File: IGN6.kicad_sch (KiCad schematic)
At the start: 24 parts

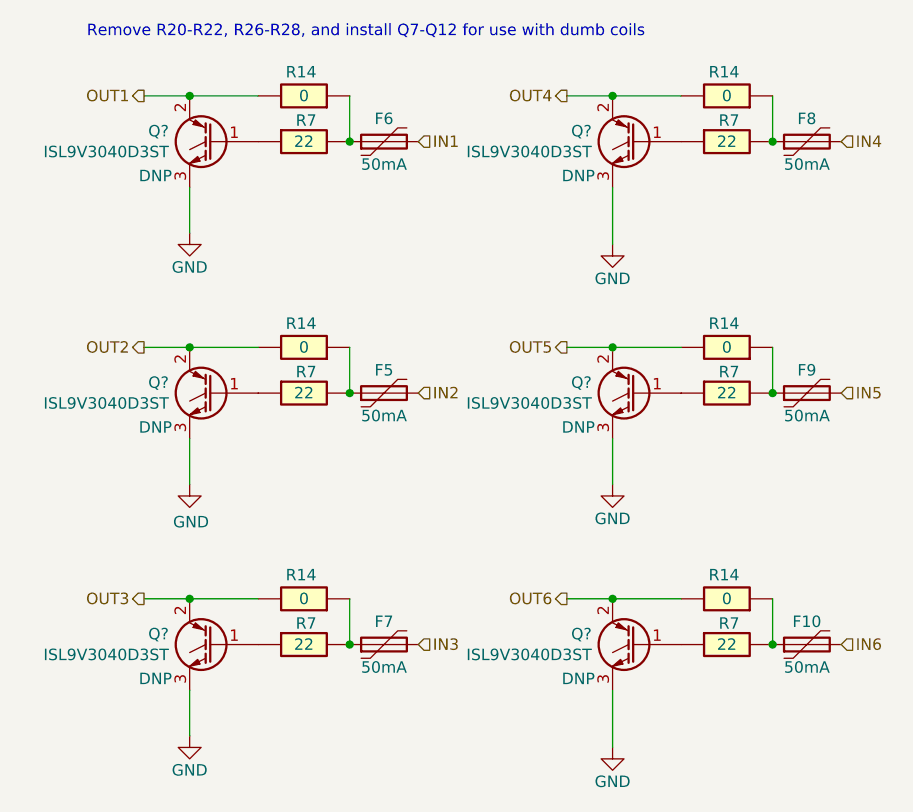
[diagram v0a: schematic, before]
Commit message: first changes from UAEFI to 4EFE ECU PCB dimensions
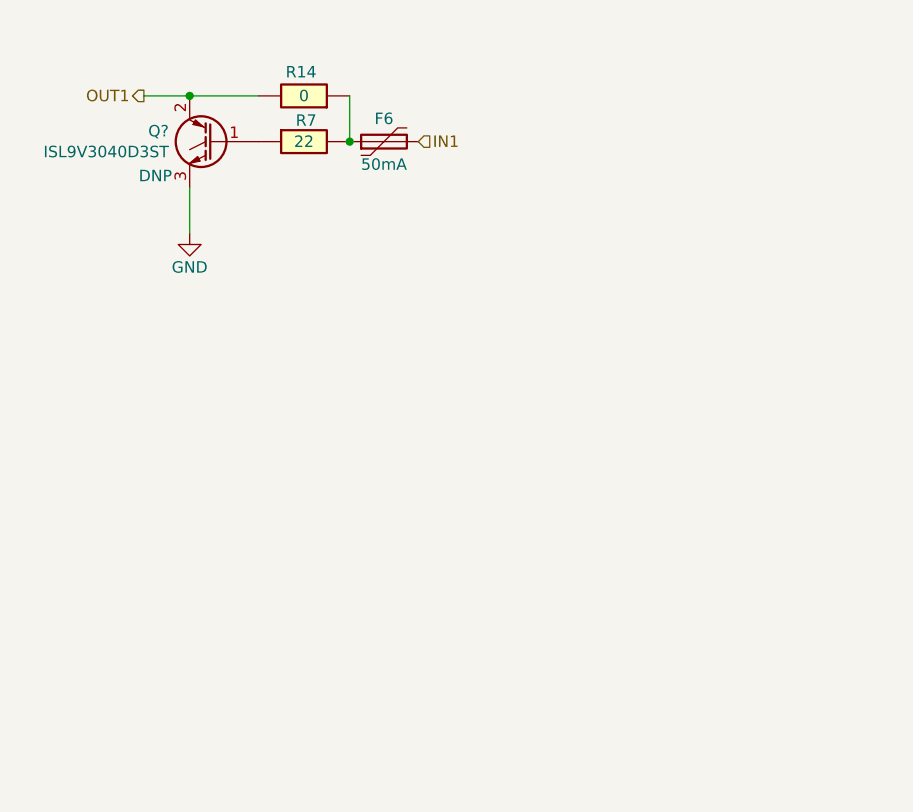
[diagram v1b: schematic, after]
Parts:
- removed F10, F5, F7, F8, F9: 50mA, Fuse:Fuse_0603_1608Metric, symbol Device:Polyfuse
- removed Q? (x5): ISL9V3040D3ST, Package_TO_SOT_SMD:TO-252-2, symbol Device:Q_NIGBT_GCE
- removed R14 (x5): 0, Resistor_SMD:R_2512_6332Metric, symbol hellen-one-common:Res
- removed R7 (x5): 22, hellen-one-common:R0603, symbol hellen-one-common:Res
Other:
- note removed: "Remove R20-R22, R26-R28, and install Q7-Q12 for use with dumb coils"
